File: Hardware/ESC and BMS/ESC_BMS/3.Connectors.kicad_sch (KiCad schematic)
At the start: 9 parts, among them J401 1mm2_connector, J402 1mm2_connector, J403 1mm2_connector, J404 JST_8PH_2mm, J405 JST_3PH_2mm, J406 1mm2_connector, J407 1mm2_connector, J408 1mm2_connector, J409 1mm2_connector

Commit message: initial BMS work
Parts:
- renumbered J409 to J10, J401 to J2, J402 to J3, J403 to J4, J404 to J5, J405 to J6, J406 to J7, J407 to J8, J408 to J9
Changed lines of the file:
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@@
 		(on_board yes)
 		(dnp no)
-		(property "Reference" "J404"
+		(property "Reference" "J5"
 			(at 89.916 30.988 0)
 			(effects
@@
 			(project ""
 				(path "/64aee9f2-a448-43ef-b28d-f00e276bd9f5/b843d17e-7d6d-4569-97d7-0fdd5bf8acb0"
-					(reference "J404")
+					(reference "J5")
 					(unit 1)
 				)
@@
 		(dnp no)
 		(fields_autoplaced yes)
-		(property "Reference" "J408"
+		(property "Reference" "J9"
 			(at 170.18 52.0699 90)
 			(effects
@@
 			(project "SPROJ3EE_ESC_BMS"
 				(path "/64aee9f2-a448-43ef-b28d-f00e276bd9f5/b843d17e-7d6d-4569-97d7-0fdd5bf8acb0"
-					(reference "J408")
+					(reference "J9")
 					(unit 1)
 				)
@@
 		(dnp no)
 		(fields_autoplaced yes)
-		(property "Reference" "J405"
+		(property "Reference" "J6"
 			(at 123.19 31.7499 0)
 			(effects
@@
 			(project ""
 				(path "/64aee9f2-a448-43ef-b28d-f00e276bd9f5/b843d17e-7d6d-4569-97d7-0fdd5bf8acb0"
-					(reference "J405")
+					(reference "J6")
 					(unit 1)
 				)
@@
 		(on_board yes)
 		(dnp no)
-		(property "Reference" "#PWR0405"
+		(property "Reference" "#PWR058"
 			(at 161.29 43.18 0)
 			(effects
@@
 			(project ""
 				(path "/64aee9f2-a448-43ef-b28d-f00e276bd9f5/b843d17e-7d6d-4569-97d7-0fdd5bf8acb0"
-					(reference "#PWR0405")
+					(reference "#PWR058")
 					(unit 1)
 				)
@@
 		(on_board yes)
 		(dnp no)
-		(property "Reference" "#PWR0407"
+		(property "Reference" "#PWR059"
 			(at 161.29 67.31 0)
 			(effects
@@
 			(project "SPROJ3EE_ESC_BMS"
 				(path "/64aee9f2-a448-43ef-b28d-f00e276bd9f5/b843d17e-7d6d-4569-97d7-0fdd5bf8acb0"
-					(reference "#PWR0407")
+					(reference "#PWR059")
 					(unit 1)
 				)
@@
 		(on_board yes)
 		(dnp no)
-		(property "Reference" "#PWR0403"
+		(property "Reference" "#PWR057"
 			(at 115.57 43.18 0)
 			(effects
@@
 			(project ""
 				(path "/64aee9f2-a448-43ef-b28d-f00e276bd9f5/b843d17e-7d6d-4569-97d7-0fdd5bf8acb0"
-					(reference "#PWR0403")
+					(reference "#PWR057")
 					(unit 1)
 				)
@@
 		(dnp no)
 		(fields_autoplaced yes)
-		(property "Reference" "J409"
+		(property "Reference" "J10"
 			(at 170.18 58.4199 90)
 			(effects
@@
 			(project "SPROJ3EE_ESC_BMS"
 				(path "/64aee9f2-a448-43ef-b28d-f00e276bd9f5/b843d17e-7d6d-4569-97d7-0fdd5bf8acb0"
-					(reference "J409")
+					(reference "J10")
 					(unit 1)
 				)
@@
 		(dnp no)
 		(fields_autoplaced yes)
-		(property "Reference" "J403"
+		(property "Reference" "J4"
 			(at 39.37 36.8299 90)
 			(effects
@@
 			(project "SPROJ3EE_ESC_BMS"
 				(path "/64aee9f2-a448-43ef-b28d-f00e276bd9f5/b843d17e-7d6d-4569-97d7-0fdd5bf8acb0"
-					(reference "J403")
+					(reference "J4")
 					(unit 1)
 				)
@@
 		(dnp no)
 		(fields_autoplaced yes)
-		(property "Reference" "J401"
+		(property "Reference" "J2"
 			(at 39.37 24.1299 90)
 			(effects
@@
 			(project ""
 				(path "/64aee9f2-a448-43ef-b28d-f00e276bd9f5/b843d17e-7d6d-4569-97d7-0fdd5bf8acb0"
-					(reference "J401")
+					(reference "J2")
 					(unit 1)
 				)
@@
 		(dnp no)
 		(fields_autoplaced yes)
-		(property "Reference" "J406"
+		(property "Reference" "J7"
 			(at 170.18 27.9399 90)
 			(effects
@@
 			(project "SPROJ3EE_ESC_BMS"
 				(path "/64aee9f2-a448-43ef-b28d-f00e276bd9f5/b843d17e-7d6d-4569-97d7-0fdd5bf8acb0"
-					(reference "J406")
+					(reference "J7")
 					(unit 1)
 				)
@@
 		(dnp no)
 		(fields_autoplaced yes)
-		(property "Reference" "J402"
+		(property "Reference" "J3"
 			(at 39.37 30.4799 90)
 			(effects
@@
 			(project "SPROJ3EE_ESC_BMS"
 				(path "/64aee9f2-a448-43ef-b28d-f00e276bd9f5/b843d17e-7d6d-4569-97d7-0fdd5bf8acb0"
-					(reference "J402")
+					(reference "J3")
 					(unit 1)
 				)
@@
 		(on_board yes)
 		(dnp no)
-		(property "Reference" "#PWR0402"
+		(property "Reference" "#PWR056"
 			(at 115.57 33.02 0)
 			(effects
@@
 			(project "SPROJ3EE_ESC_BMS"
 				(path "/64aee9f2-a448-43ef-b28d-f00e276bd9f5/b843d17e-7d6d-4569-97d7-0fdd5bf8acb0"
-					(reference "#PWR0402")
+					(reference "#PWR056")
 					(unit 1)
 				)
@@
 		(dnp no)
 		(fields_autoplaced yes)
-		(property "Reference" "J407"
+		(property "Reference" "J8"
 			(at 170.18 34.2899 90)
 			(effects
@@
 			(project "SPROJ3EE_ESC_BMS"
 				(path "/64aee9f2-a448-43ef-b28d-f00e276bd9f5/b843d17e-7d6d-4569-97d7-0fdd5bf8acb0"
-					(reference "J407")
+					(reference "J8")
 					(unit 1)
 				)
@@
 		(on_board yes)
 		(dnp no)
-		(property "Reference" "#PWR0401"
+		(property "Reference" "#PWR055"
 			(at 107.95 33.02 0)
 			(effects
@@
 			(project ""
 				(path "/64aee9f2-a448-43ef-b28d-f00e276bd9f5/b843d17e-7d6d-4569-97d7-0fdd5bf8acb0"
-					(reference "#PWR0401")
-					(unit 1)
-				)
+					(reference "#PWR055")
+					(unit 1)
+				)

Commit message: more BMS
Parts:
- removed J10, J7, J8, J9: 1mm2_connector, Connector_Wire:SolderWire-1sqmm_1x01_D1.4mm_OD2.7mm, symbol Mechanical:MountingHole_Pad
- added J11, J12, J13, J14: 1mm2_connector, Connector_Wire:SolderWire-1sqmm_1x01_D1.4mm_OD2.7mm, symbol Mechanical:MountingHole_Pad
- added J11: Jack-DC, symbol Connector:Jack-DC
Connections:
- net +VBATT: now also J11.1
- net GND: now also J11.2, J14.1
- new net DC: J11.1
- new net VMID: J12.1, J13.1

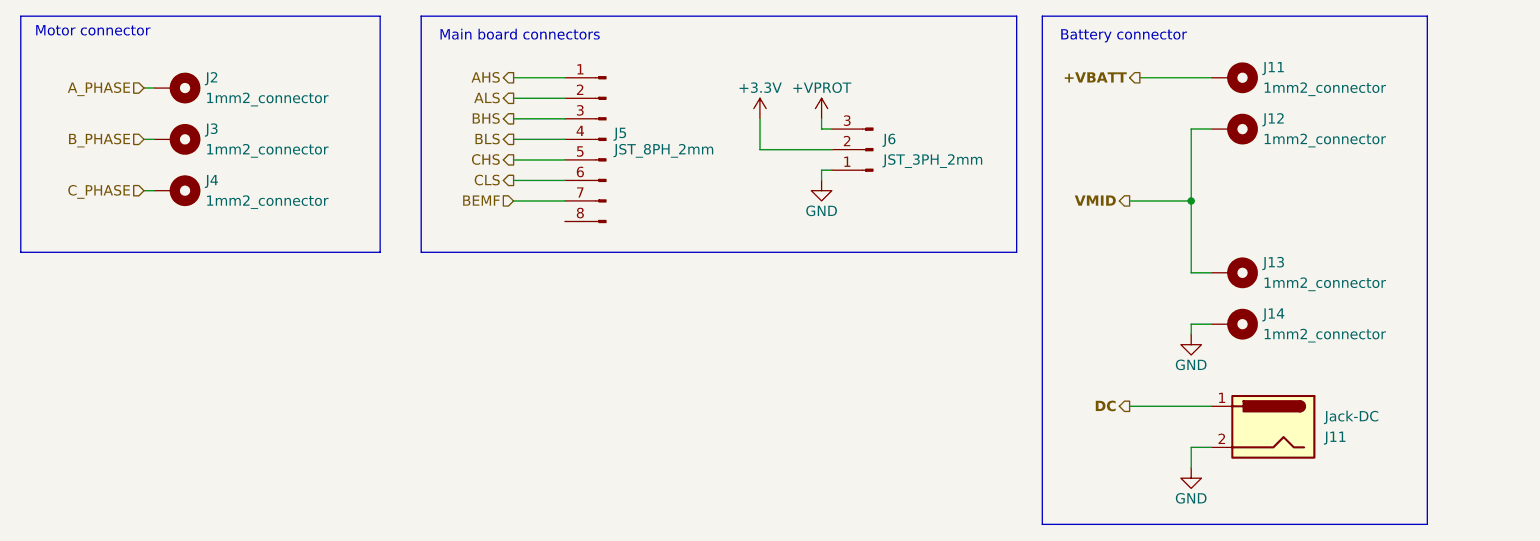
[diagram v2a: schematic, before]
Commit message: Simulations for BMS start and footprints
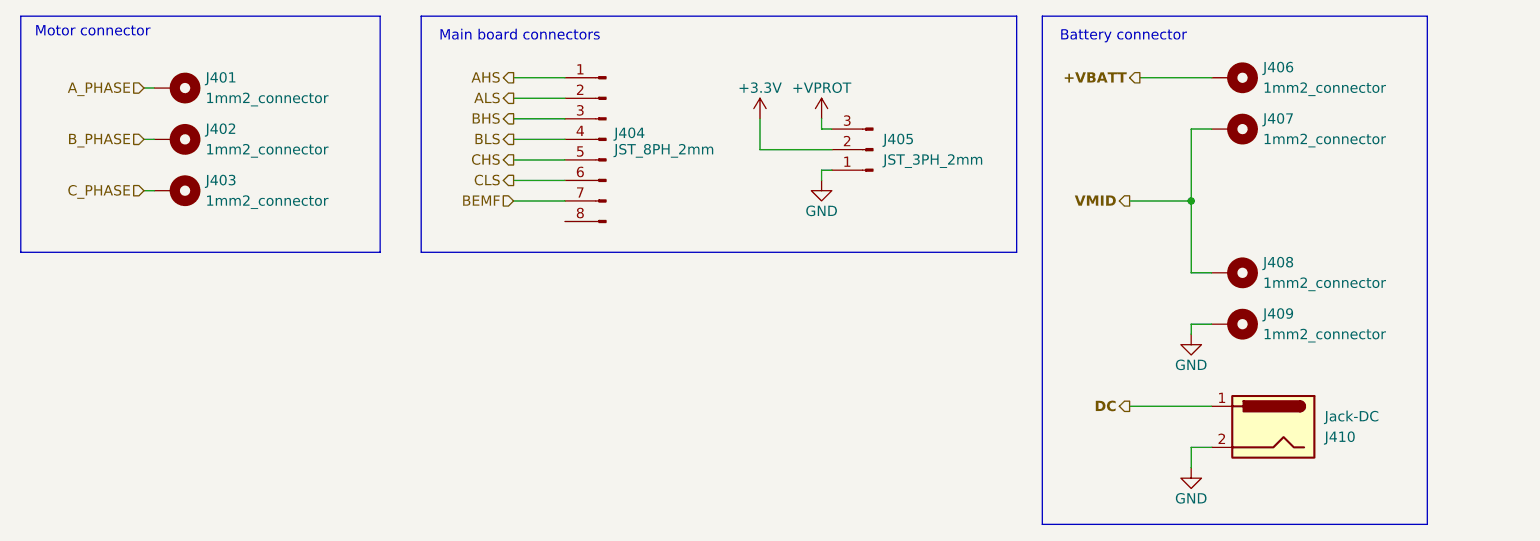
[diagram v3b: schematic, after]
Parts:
- renumbered J2 to J401, J3 to J402, J4 to J403, J5 to J404, J6 to J405, J11 to J406, J12 to J407, J13 to J408, J14 to J409, J11 to J410
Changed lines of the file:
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@@
 		(dnp no)
 		(fields_autoplaced yes)
-		(property "Reference" "J11"
+		(property "Reference" "J406"
 			(at 170.18 22.8599 90)
 			(effects
@@
 			(project "SPROJ3EE_ESC_BMS"
 				(path "/64aee9f2-a448-43ef-b28d-f00e276bd9f5/b843d17e-7d6d-4569-97d7-0fdd5bf8acb0"
-					(reference "J11")
+					(reference "J406")
 					(unit 1)
 				)
@@
 		(on_board yes)
 		(dnp no)
-		(property "Reference" "J5"
+		(property "Reference" "J404"
 			(at 89.916 30.988 0)
 			(effects
@@
 			(project ""
 				(path "/64aee9f2-a448-43ef-b28d-f00e276bd9f5/b843d17e-7d6d-4569-97d7-0fdd5bf8acb0"
-					(reference "J5")
+					(reference "J404")
 					(unit 1)
 				)
@@
 		(dnp no)
 		(fields_autoplaced yes)
-		(property "Reference" "J6"
+		(property "Reference" "J405"
 			(at 123.19 31.7499 0)
 			(effects
@@
 			(project ""
 				(path "/64aee9f2-a448-43ef-b28d-f00e276bd9f5/b843d17e-7d6d-4569-97d7-0fdd5bf8acb0"
-					(reference "J6")
+					(reference "J405")
 					(unit 1)
 				)
@@
 		(dnp no)
 		(fields_autoplaced yes)
-		(property "Reference" "J14"
+		(property "Reference" "J409"
 			(at 170.18 53.3399 90)
 			(effects
@@
 			(project "SPROJ3EE_ESC_BMS"
 				(path "/64aee9f2-a448-43ef-b28d-f00e276bd9f5/b843d17e-7d6d-4569-97d7-0fdd5bf8acb0"
-					(reference "J14")
+					(reference "J409")
 					(unit 1)
 				)
@@
 		(on_board yes)
 		(dnp no)
-		(property "Reference" "#PWR072"
+		(property "Reference" "#PWR0403"
 			(at 115.57 43.18 0)
 			(effects
@@
 			(project ""
 				(path "/64aee9f2-a448-43ef-b28d-f00e276bd9f5/b843d17e-7d6d-4569-97d7-0fdd5bf8acb0"
-					(reference "#PWR072")
+					(reference "#PWR0403")
 					(unit 1)
 				)
@@
 		(dnp no)
 		(fields_autoplaced yes)
-		(property "Reference" "J12"
+		(property "Reference" "J407"
 			(at 170.18 29.2099 90)
 			(effects
@@
 			(project "SPROJ3EE_ESC_BMS"
 				(path "/64aee9f2-a448-43ef-b28d-f00e276bd9f5/b843d17e-7d6d-4569-97d7-0fdd5bf8acb0"
-					(reference "J12")
+					(reference "J407")
 					(unit 1)
 				)
@@
 		(on_board yes)
 		(dnp no)
-		(property "Reference" "#PWR073"
+		(property "Reference" "#PWR0404"
 			(at 161.29 62.23 0)
 			(effects
@@
 			(project "SPROJ3EE_ESC_BMS"
 				(path "/64aee9f2-a448-43ef-b28d-f00e276bd9f5/b843d17e-7d6d-4569-97d7-0fdd5bf8acb0"
-					(reference "#PWR073")
+					(reference "#PWR0404")
 					(unit 1)
 				)
@@
 		(on_board yes)
 		(dnp no)
-		(property "Reference" "#PWR074"
+		(property "Reference" "#PWR0405"
 			(at 161.29 78.74 0)
 			(effects
@@
 			(project "SPROJ3EE_ESC_BMS"
 				(path "/64aee9f2-a448-43ef-b28d-f00e276bd9f5/b843d17e-7d6d-4569-97d7-0fdd5bf8acb0"
-					(reference "#PWR074")
+					(reference "#PWR0405")
 					(unit 1)
 				)
@@
 		(on_board yes)
 		(dnp no)
-		(property "Reference" "J11"
+		(property "Reference" "J410"
 			(at 177.8 68.5801 0)
 			(effects
@@
 			(project ""
 				(path "/64aee9f2-a448-43ef-b28d-f00e276bd9f5/b843d17e-7d6d-4569-97d7-0fdd5bf8acb0"
-					(reference "J11")
+					(reference "J410")
 					(unit 1)
 				)
@@
 		(dnp no)
 		(fields_autoplaced yes)
-		(property "Reference" "J4"
+		(property "Reference" "J403"
 			(at 39.37 36.8299 90)
 			(effects
@@
 			(project "SPROJ3EE_ESC_BMS"
 				(path "/64aee9f2-a448-43ef-b28d-f00e276bd9f5/b843d17e-7d6d-4569-97d7-0fdd5bf8acb0"
-					(reference "J4")
+					(reference "J403")
 					(unit 1)
 				)
@@
 		(dnp no)
 		(fields_autoplaced yes)
-		(property "Reference" "J2"
+		(property "Reference" "J401"
 			(at 39.37 24.1299 90)
 			(effects
@@
 			(project ""
 				(path "/64aee9f2-a448-43ef-b28d-f00e276bd9f5/b843d17e-7d6d-4569-97d7-0fdd5bf8acb0"
-					(reference "J2")
+					(reference "J401")
 					(unit 1)
 				)
@@
 		(dnp no)
 		(fields_autoplaced yes)
-		(property "Reference" "J3"
+		(property "Reference" "J402"
 			(at 39.37 30.4799 90)
 			(effects
@@
 			(project "SPROJ3EE_ESC_BMS"
 				(path "/64aee9f2-a448-43ef-b28d-f00e276bd9f5/b843d17e-7d6d-4569-97d7-0fdd5bf8acb0"
-					(reference "J3")
+					(reference "J402")
 					(unit 1)
 				)
@@
 		(dnp no)
 		(fields_autoplaced yes)
-		(property "Reference" "J13"
+		(property "Reference" "J408"
 			(at 170.18 46.9899 90)
 			(effects
@@
 			(project "SPROJ3EE_ESC_BMS"
 				(path "/64aee9f2-a448-43ef-b28d-f00e276bd9f5/b843d17e-7d6d-4569-97d7-0fdd5bf8acb0"
-					(reference "J13")
+					(reference "J408")
 					(unit 1)
 				)
@@
 		(on_board yes)
 		(dnp no)
-		(property "Reference" "#PWR071"
+		(property "Reference" "#PWR0402"
 			(at 115.57 33.02 0)
 			(effects
@@
 			(project "SPROJ3EE_ESC_BMS"
 				(path "/64aee9f2-a448-43ef-b28d-f00e276bd9f5/b843d17e-7d6d-4569-97d7-0fdd5bf8acb0"
-					(reference "#PWR071")
+					(reference "#PWR0402")
 					(unit 1)
 				)
@@
 		(on_board yes)
 		(dnp no)
-		(property "Reference" "#PWR070"
+		(property "Reference" "#PWR0401"
 			(at 107.95 33.02 0)
 			(effects
@@
 			(project ""
 				(path "/64aee9f2-a448-43ef-b28d-f00e276bd9f5/b843d17e-7d6d-4569-97d7-0fdd5bf8acb0"
-					(reference "#PWR070")
-					(unit 1)
-				)
+					(reference "#PWR0401")
+					(unit 1)
+				)

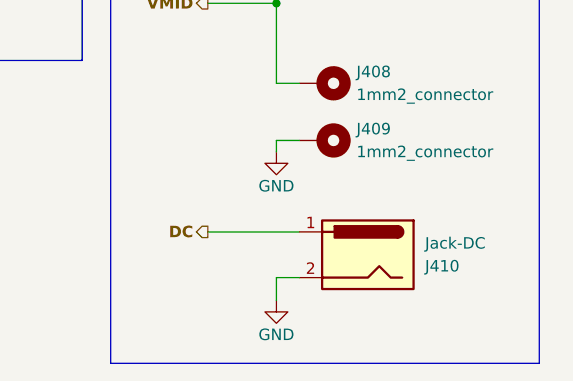
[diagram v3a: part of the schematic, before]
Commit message: More BMS
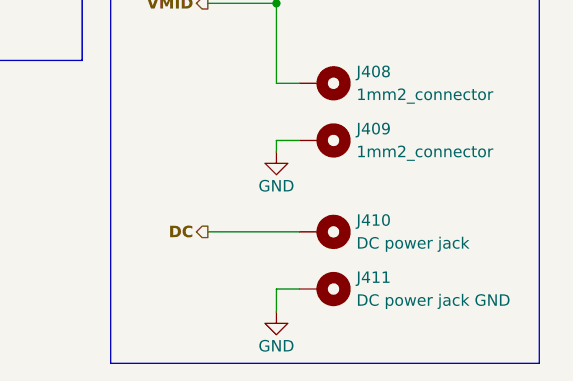
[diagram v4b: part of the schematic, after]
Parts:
- removed J410: Jack-DC, symbol Connector:Jack-DC
- added J410: DC power jack, Connector_Wire:SolderWire-1sqmm_1x01_D1.4mm_OD2.7mm, symbol Mechanical:MountingHole_Pad
- added J411: DC power jack GND, Connector_Wire:SolderWire-1sqmm_1x01_D1.4mm_OD2.7mm, symbol Mechanical:MountingHole_Pad
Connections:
- net DC: now also J410.1
- net GND: now also J411.1
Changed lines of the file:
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@@
 	(wire
 		(pts
-			(xy 161.29 69.85) (xy 163.83 69.85)
+			(xy 161.29 71.12) (xy 163.83 71.12)
 		)
 		(stroke
@@
 	(wire
 		(pts
-			(xy 161.29 69.85) (xy 161.29 72.39)
+			(xy 161.29 71.12) (xy 161.29 73.66)
 		)
 		(stroke
@@
 			)
 			(justify right)
+		)
+	)
+	(symbol
+		(lib_id "Mechanical:MountingHole_Pad")
+		(at 166.37 71.12 270)
+		(unit 1)
+		(exclude_from_sim no)
+		(in_bom no)
+		(on_board yes)
+		(dnp no)
+		(fields_autoplaced yes)
+		(property "Reference" "J411"
+			(at 170.18 69.8499 90)
+			(effects
+				(font
+					(size 1.27 1.27)
+				)
+				(justify left)
+			)
+		)
+		(property "Value" "DC power jack GND"
+			(at 170.18 72.3899 90)
+			(effects
+				(font
+					(size 1.27 1.27)
+				)
+				(justify left)
+			)
+		)
+		(property "Footprint" "Connector_Wire:SolderWire-1sqmm_1x01_D1.4mm_OD2.7mm"
+			(at 166.37 71.12 0)
+			(effects
+				(font
+					(size 1.27 1.27)
+				)
+				(hide yes)
+			)
+		)
+		(property "Datasheet" "~"
+			(at 166.37 71.12 0)
+			(effects
+				(font
+					(size 1.27 1.27)
+				)
+				(hide yes)
+			)
+		)
+		(property "Description" "Mounting Hole with connection"
+			(at 166.37 71.12 0)
+			(effects
+				(font
+					(size 1.27 1.27)
+				)
+				(hide yes)
+			)
+		)
+		(pin "1"
+		)
+		(instances
+			(project "SPROJ3EE_ESC_BMS"
+				(path "/64aee9f2-a448-43ef-b28d-f00e276bd9f5/b843d17e-7d6d-4569-97d7-0fdd5bf8acb0"
+					(reference "J411")
+					(unit 1)
+				)
+			)
 		)
 	)
@@
 	)
 	(symbol
+		(lib_id "Mechanical:MountingHole_Pad")
+		(at 166.37 64.77 270)
+		(unit 1)
+		(exclude_from_sim no)
+		(in_bom no)
+		(on_board yes)
+		(dnp no)
+		(fields_autoplaced yes)
+		(property "Reference" "J410"
+			(at 170.18 63.4999 90)
+			(effects
+				(font
+					(size 1.27 1.27)
+				)
+				(justify left)
+			)
+		)
+		(property "Value" "DC power jack"
+			(at 170.18 66.0399 90)
+			(effects
+				(font
+					(size 1.27 1.27)
+				)
+				(justify left)
+			)
+		)
+		(property "Footprint" "Connector_Wire:SolderWire-1sqmm_1x01_D1.4mm_OD2.7mm"
+			(at 166.37 64.77 0)
+			(effects
+				(font
+					(size 1.27 1.27)
+				)
+				(hide yes)
+			)
+		)
+		(property "Datasheet" "~"
+			(at 166.37 64.77 0)
+			(effects
+				(font
+					(size 1.27 1.27)
+				)
+				(hide yes)
+			)
+		)
+		(property "Description" "Mounting Hole with connection"
+			(at 166.37 64.77 0)
+			(effects
+				(font
+					(size 1.27 1.27)
+				)
+				(hide yes)
+			)
+		)
+		(pin "1"
+		)
+		(instances
+			(project "SPROJ3EE_ESC_BMS"
+				(path "/64aee9f2-a448-43ef-b28d-f00e276bd9f5/b843d17e-7d6d-4569-97d7-0fdd5bf8acb0"
+					(reference "J410")
+					(unit 1)
+				)
+			)
+		)
+	)
+	(symbol
 		(lib_id "power:GND")
-		(at 161.29 72.39 0)
+		(at 161.29 73.66 0)
 		(unit 1)
 		(exclude_from_sim no)
@@
 		(dnp no)
 		(property "Reference" "#PWR0405"
-			(at 161.29 78.74 0)
+			(at 161.29 80.01 0)
 			(effects
 				(font
@@
 		)
 		(property "Value" "GND"
-			(at 161.29 76.2 0)
+			(at 161.29 77.47 0)
 			(effects
 				(font
@@
 		)
 		(property "Footprint" ""
-			(at 161.29 72.39 0)
+			(at 161.29 73.66 0)
 			(effects
 				(font
@@
 		)
 		(property "Datasheet" ""
-			(at 161.29 72.39 0)
+			(at 161.29 73.66 0)
 			(effects
 				(font
@@
 		)
 		(property "Description" "Power symbol creates a global label with name \"GND\" , ground"
-			(at 161.29 72.39 0)
+			(at 161.29 73.66 0)
 			(effects
 				(font
@@
 					(unit 1)
 				)
-			)
-		)
-	)
-	(symbol
-		(lib_id "Connector:Jack-DC")
-		(at 171.45 67.31 0)
-		(mirror y)
-		(unit 1)
-		(exclude_from_sim no)
-		(in_bom yes)
-		(on_board yes)
-		(dnp no)
-		(property "Reference" "J410"
-			(at 177.8 68.5801 0)
-			(effects
-				(font
-					(size 1.27 1.27)
-				)
-				(justify right)
-			)
-		)
-		(property "Value" "Jack-DC"
-			(at 177.8 66.0401 0)
-			(effects
-				(font
-					(size 1.27 1.27)
-				)
-				(justify right)
-			)
-		)
-		(property "Footprint" ""
-			(at 170.18 68.326 0)
-			(effects
-				(font
-					(size 1.27 1.27)
-				)
-				(hide yes)
-			)
-		)
-		(property "Datasheet" "~"
-			(at 170.18 68.326 0)
-			(effects
-				(font
-					(size 1.27 1.27)
-				)
-				(hide yes)
-			)
-		)
-		(property "Description" "DC Barrel Jack"
-			(at 171.45 67.31 0)
-			(effects
-				(font
-					(size 1.27 1.27)
-				)
-				(hide yes)
-			)
-		)
-		(pin "1"
-		)
-		(pin "2"
-		)
-		(instances
-			(project ""
-				(path "/64aee9f2-a448-43ef-b28d-f00e276bd9f5/b843d17e-7d6d-4569-97d7-0fdd5bf8acb0"
-					(reference "J410")
-					(unit 1)
-				)
